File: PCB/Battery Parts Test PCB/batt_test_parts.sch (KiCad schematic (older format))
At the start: 13 parts

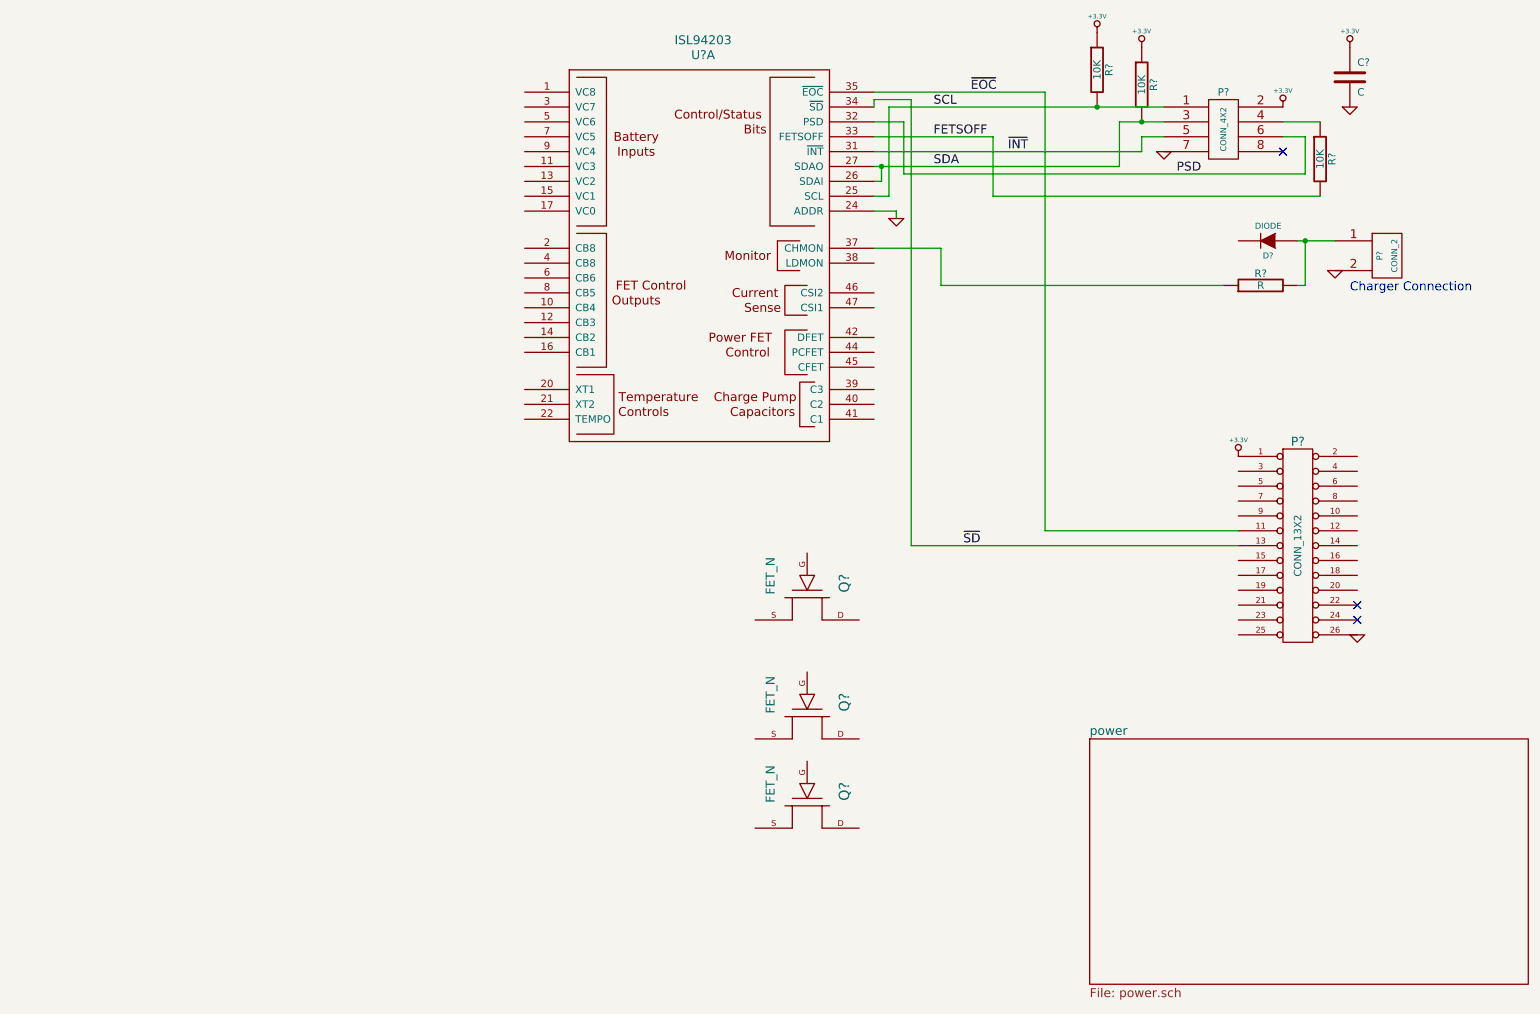
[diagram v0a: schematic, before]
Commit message: first draft schematic complete for bat mon
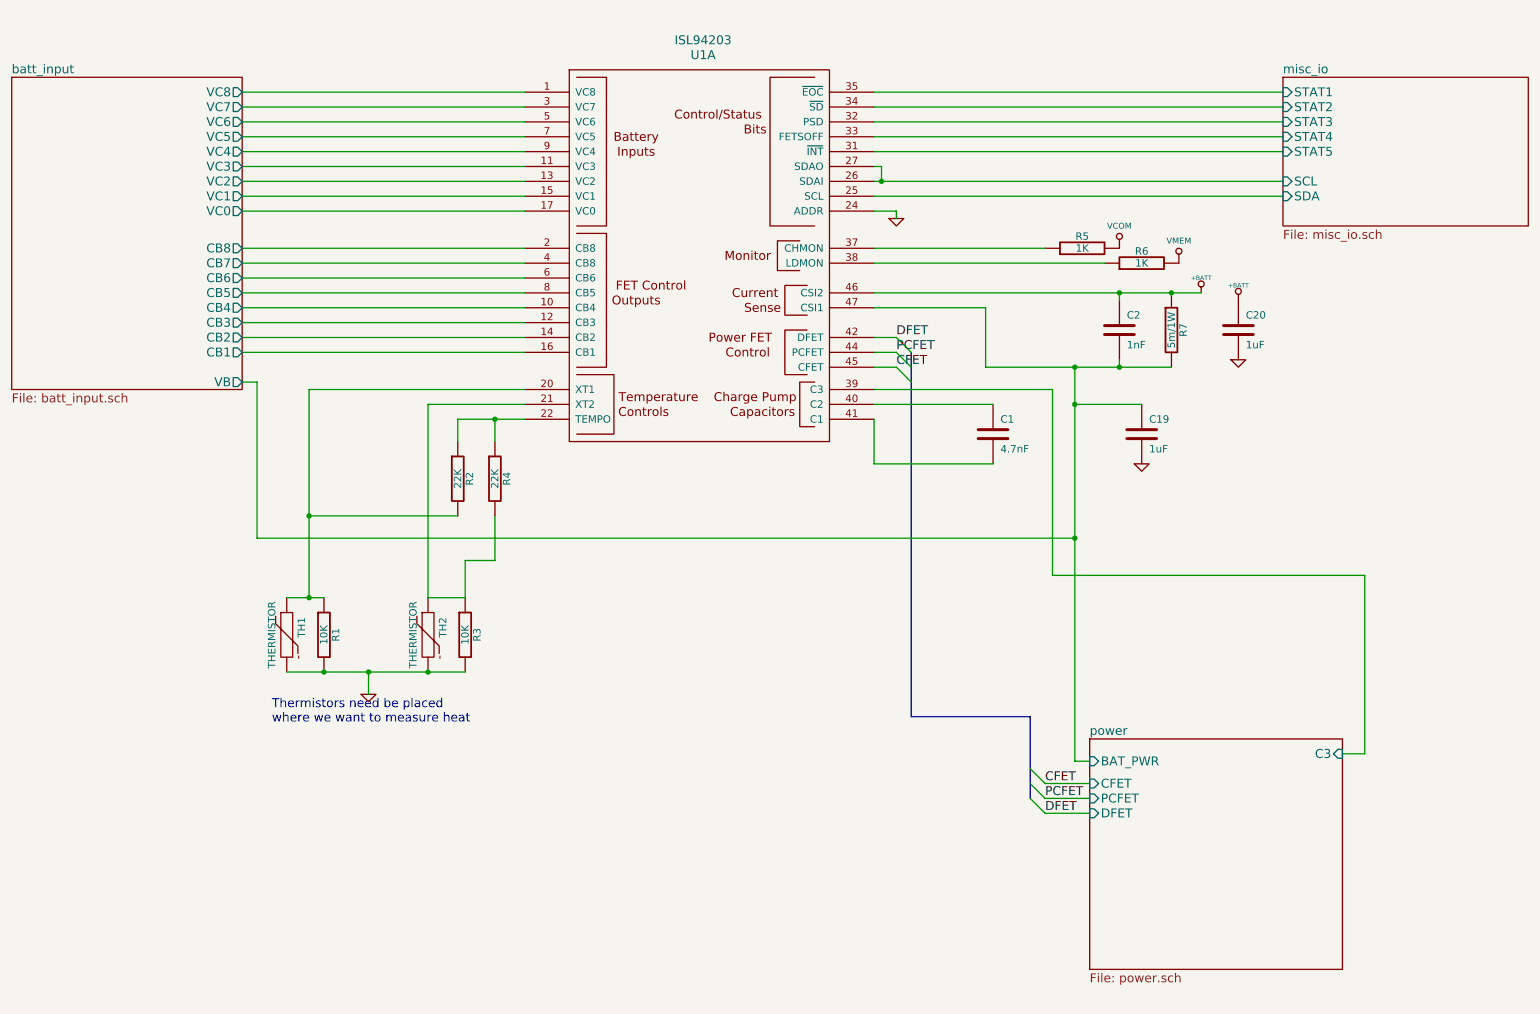
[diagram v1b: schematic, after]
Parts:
- removed C?: C, symbol C
- removed D?: DIODE, symbol DIODE
- removed P?: CONN_4X2, symbol CONN_4X2
- removed P?: CONN_13X2, symbol CONN_13X2
- removed P?: CONN_2, symbol CONN_2
- removed Q? (x3): FET_N, symbol FET_N
- removed R? (x3): 10K, symbol R
- removed R?: R, symbol R
- added C1: 4.7nF, symbol C
- added C19, C20: 1uF, symbol C
- added C2: 1nF, symbol C
- added R1, R3: 10K, symbol R
- added R2, R4: 22K, symbol R
- added R5, R6: 1K, symbol R
- added R7: 5m/1W, symbol R
- added TH1, TH2: THERMISTOR, symbol THERMISTOR
- gave numbers to parts that had none: 1
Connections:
- net GND: now also C19.2, C20.2, R1.2, R3.2, TH1.2, TH2.2
- net batt_input/VC8: now reaches U1.1 (VC8)
- net batt_input/CB4: now reaches U1.10 (CB4)
- net batt_input/VC3: now reaches U1.11 (VC3)
- net batt_input/CB3: now reaches U1.12 (CB3)
- net batt_input/VC2: now reaches U1.13 (VC2)
- net batt_input/CB2: now reaches U1.14 (CB2)
- net batt_input/VC1: now reaches U1.15 (VC1)
- net batt_input/CB1: now reaches U1.16 (CB1)
- net batt_input/VC0: now reaches U1.17 (VC0)
- net batt_input/CB8: now reaches U1.2 (CB8)
- net at U1.20 (XT1): now also R1.1, R2.2, TH1.1
- net at U1.21 (XT2): now also R3.1, R4.2, TH2.1
- net at U1.22 (TEMPO): now also R2.1, R4.1
- net batt_input/VC7: now reaches U1.3 (VC7)
- net at U1.37 (CHMON): now also R5.1
- net at U1.38 (LDMON): now also R6.1
- net power/C3: now reaches U1.39 (C3)
- net batt_input/CB7: now reaches U1.4 (CB8)
- net at U1.40 (C2): now also C1.1
- net at U1.41 (C1): now also C1.2
- net DFET: now reaches U1.42 (DFET)
- net PCFET: now reaches U1.44 (PCFET)
- net CFET: now reaches U1.45 (CFET)
- net +BATT: now reaches U1.46 (CSI2)
- net +BATT: now also C2.1, C20.1, R7.1
- net batt_input/VB: now reaches U1.47 (CSI1)
- net batt_input/VB: now also C19.1, C2.2, R7.2
- net batt_input/VC6: now reaches U1.5 (VC6)
- net batt_input/CB6: now reaches U1.6 (CB6)
- net batt_input/VC5: now reaches U1.7 (VC5)
- net batt_input/CB5: now reaches U1.8 (CB5)
- net batt_input/VC4: now reaches U1.9 (VC4)
- net FETSOFF renamed misc_io/STAT4
- net PSD renamed misc_io/STAT3
- net SCL renamed misc_io/SDA
- net SDA renamed misc_io/SCL
- net ~EOC renamed misc_io/STAT1
- net ~INT renamed misc_io/STAT5
- net ~SD renamed misc_io/STAT2
- new net VCOM: R5.2
- new net VMEM: R6.2
- no-connect marks 3 -> 0
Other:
- note added: "Thermistors need be placed \nwhere we want to measure heat"
- note removed: "Charger Connection"
